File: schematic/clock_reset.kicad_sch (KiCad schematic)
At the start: 13 parts, among them U22 74LS04, U7 74LS05

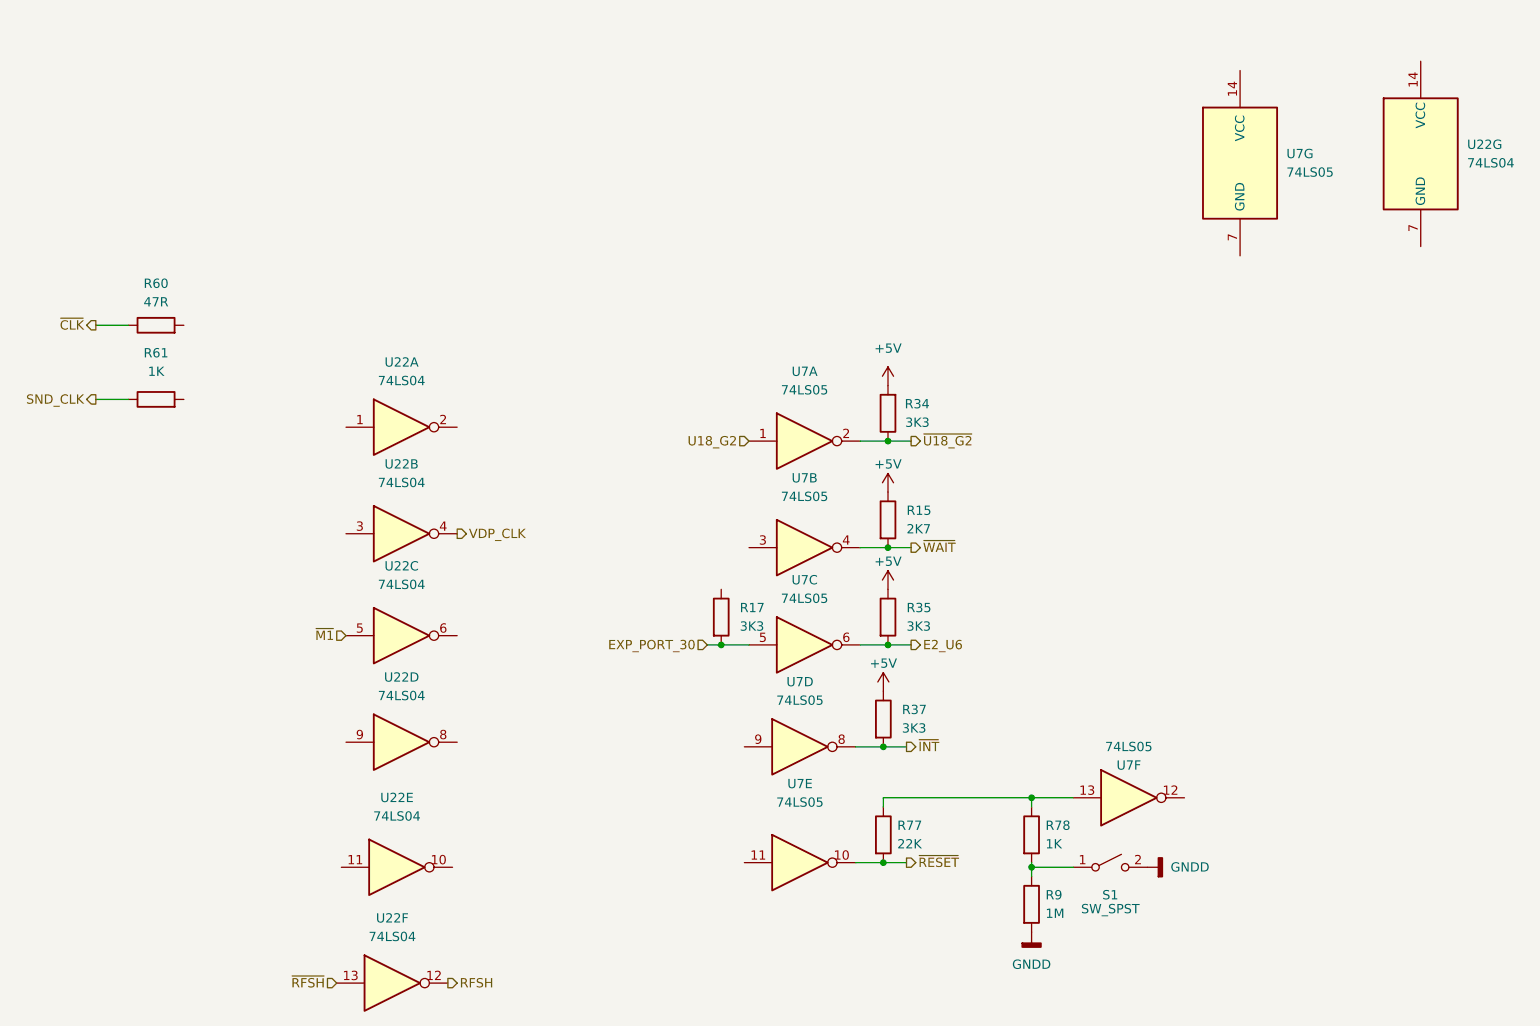
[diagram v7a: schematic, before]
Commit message: power supply added, controller circuit added. Controller is a very odd duck to say the least. Seems they wanted to have plenty of current, maybe due to the steering wheel attachement?
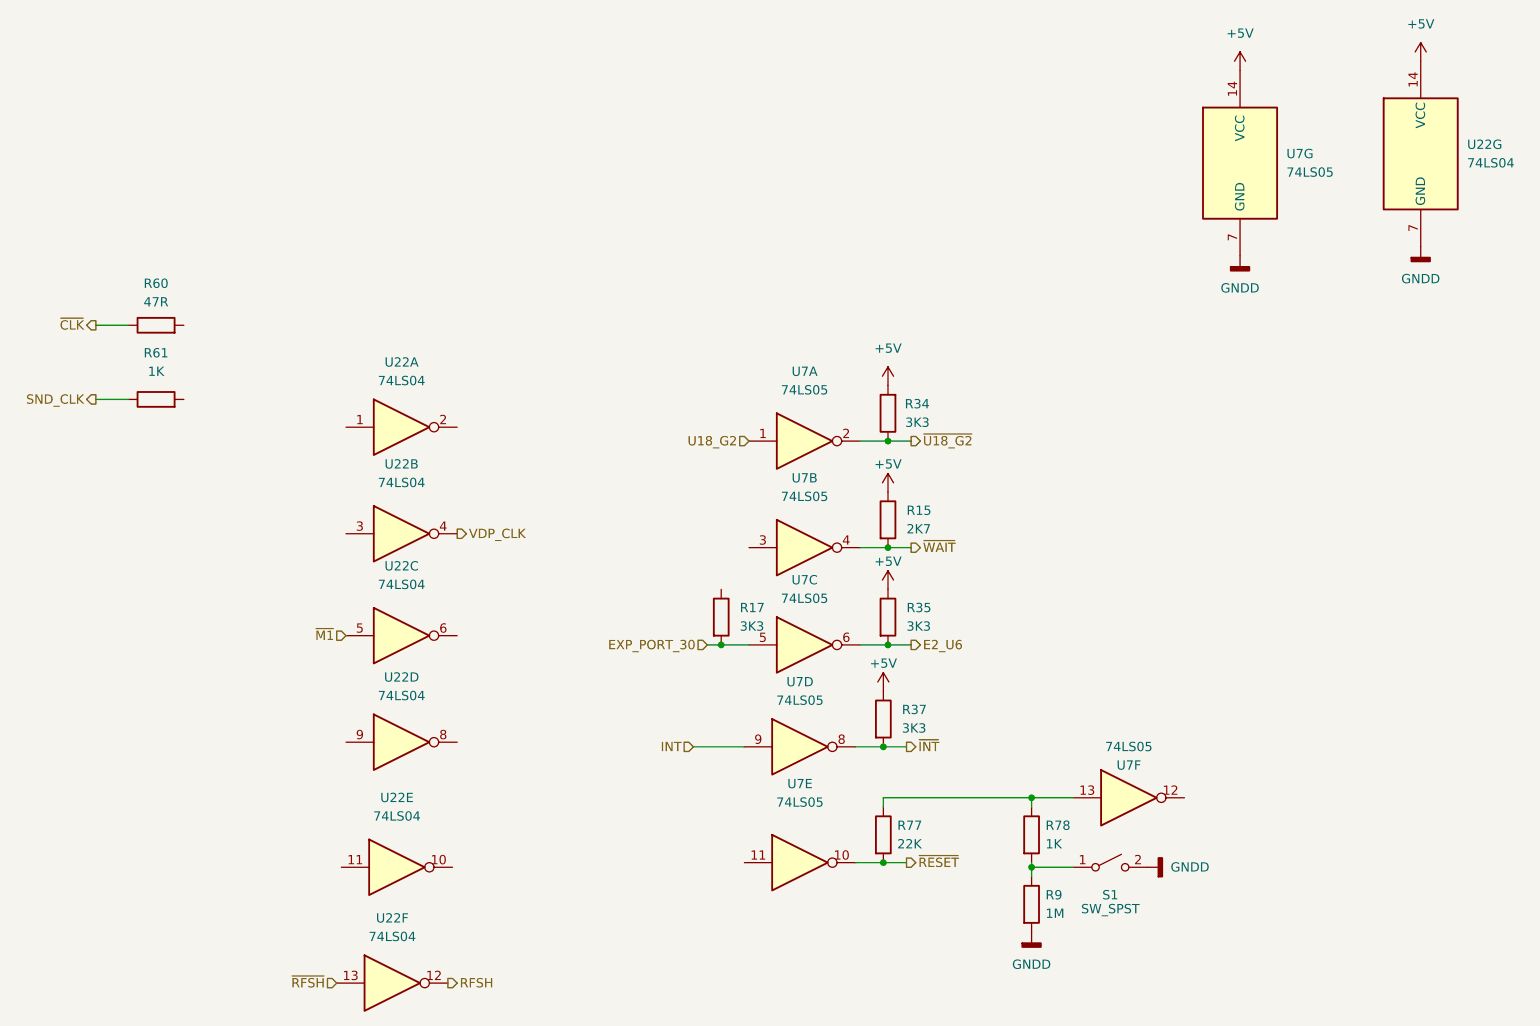
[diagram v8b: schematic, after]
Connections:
- net +5V: now also U22.14 (VCC), U7.14 (VCC)
- net GNDD: now also U22.7 (GND), U7.7 (GND)
- net INT: now reaches U7.9
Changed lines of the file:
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@@
+    (stroke (width 0) (type default) (color 0 0 0 0))
+  )
+  (wire (pts (xy 156.21 128.905) (xy 163.195 128.905))
     (stroke (width 0) (type default) (color 0 0 0 0))
   )
@@
     (effects (font (size 1.27 1.27)) (justify left))
   )
+  (hierarchical_label "INT" (shape input) (at 156.21 128.905 180)
+    (effects (font (size 1.27 1.27)) (justify right))
+  )
   (hierarchical_label "~{M1}" (shape input) (at 108.585 113.665 180)
     (effects (font (size 1.27 1.27)) (justify right))
@@
     (pin "1")
   )
+  (symbol (lib_id "power:GNDD") (at 231.14 61.595 0) (unit 1)
+    (in_bom yes) (on_board yes) (fields_autoplaced)
+    (property "Reference" "#PWR?" (id 0) (at 231.14 67.945 0)
+      (effects (font (size 1.27 1.27)) hide)
+    )
+    (property "Value" "GNDD" (id 1) (at 231.14 66.04 0))
+    (property "Footprint" "" (id 2) (at 231.14 61.595 0)
+      (effects (font (size 1.27 1.27)) hide)
+    )
+    (property "Datasheet" "" (id 3) (at 231.14 61.595 0)
+      (effects (font (size 1.27 1.27)) hide)
+    )
+    (pin "1")
+  )
   (symbol (lib_id "power:GNDD") (at 202.565 154.305 0) (unit 1)
     (in_bom yes) (on_board yes) (fields_autoplaced)
@@
     )
     (property "Datasheet" "" (id 3) (at 202.565 154.305 0)
+      (effects (font (size 1.27 1.27)) hide)
+    )
+    (pin "1")
+  )
+  (symbol (lib_id "power:GNDD") (at 255.905 60.325 0) (unit 1)
+    (in_bom yes) (on_board yes) (fields_autoplaced)
+    (property "Reference" "#PWR?" (id 0) (at 255.905 66.675 0)
+      (effects (font (size 1.27 1.27)) hide)
+    )
+    (property "Value" "GNDD" (id 1) (at 255.905 64.77 0))
+    (property "Footprint" "" (id 2) (at 255.905 60.325 0)
+      (effects (font (size 1.27 1.27)) hide)
+    )
+    (property "Datasheet" "" (id 3) (at 255.905 60.325 0)
       (effects (font (size 1.27 1.27)) hide)
     )
@@
     (pin "2")
   )
+  (symbol (lib_id "power:+5V") (at 231.14 36.195 0) (unit 1)
+    (in_bom yes) (on_board yes) (fields_autoplaced)
+    (property "Reference" "#PWR?" (id 0) (at 231.14 40.005 0)
+      (effects (font (size 1.27 1.27)) hide)
+    )
+    (property "Value" "+5V" (id 1) (at 231.14 31.115 0))
+    (property "Footprint" "" (id 2) (at 231.14 36.195 0)
+      (effects (font (size 1.27 1.27)) hide)
+    )
+    (property "Datasheet" "" (id 3) (at 231.14 36.195 0)
+      (effects (font (size 1.27 1.27)) hide)
+    )
+    (pin "1")
+  )
+  (symbol (lib_id "power:+5V") (at 255.905 34.925 0) (unit 1)
+    (in_bom yes) (on_board yes) (fields_autoplaced)
+    (property "Reference" "#PWR?" (id 0) (at 255.905 38.735 0)
+      (effects (font (size 1.27 1.27)) hide)
+    )
+    (property "Value" "+5V" (id 1) (at 255.905 29.845 0))
+    (property "Footprint" "" (id 2) (at 255.905 34.925 0)
+      (effects (font (size 1.27 1.27)) hide)
+    )
+    (property "Datasheet" "" (id 3) (at 255.905 34.925 0)
+      (effects (font (size 1.27 1.27)) hide)
+    )
+    (pin "1")
+  )
   (symbol (lib_id "74xx:74LS04") (at 116.205 99.695 0) (unit 2)
